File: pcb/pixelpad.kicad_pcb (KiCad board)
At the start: 2 copper layers, 61.5 x 55.5 mm, 17 parts, among them J1 OLED Display, SW1 SW_Push_45deg, SW2 SW_Push_45deg, SW3 RotaryEncoder_Switch, SW4 SW_Push_45deg, SW5 SW_Push_45deg, SW6 SW_Push_45deg, U1 MOUDLE-SEEEDUINO-XIAO

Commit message: The pins on the pcb for the oled were flipped for some reason
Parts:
- moved J1 7.50 mm to (59.0, 46.0), turned to 180 degrees
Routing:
- net GND: track 86.3 -> 89.6 mm, vias 2 -> 1
- net VCC: track 65.5 -> 66.5 mm
- net SDA: track 40.0 -> 39.2 mm, vias 0 -> 1
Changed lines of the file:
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@@
 	(footprint "Connector_PinHeader_2.54mm:PinHeader_1x04_P2.54mm_Vertical"
 		(layer "F.Cu")
-		(at 59 38.5)
+		(at 59 46 180)
 		(descr "Through hole straight pin header, 1x04, 2.54mm pitch, single row")
 		(tags "Through hole pin header THT 1x04 2.54mm single row")
@@
 		(duplicate_pad_numbers_are_jumpers no)
 		(fp_line
-			(start -1.38 -1.38)
-			(end 0 -1.38)
+			(start 1.38 1.27)
+			(end 1.38 9)
 			(stroke
 				(width 0.12)
@@
 		)
 		(fp_line
-			(start -1.38 0)
-			(end -1.38 -1.38)
+			(start -1.38 9)
+			(end 1.38 9)
 			(stroke
 				(width 0.12)
@@
 		(fp_line
 			(start -1.38 1.27)
-			(end -1.38 9)
+			(end 1.38 1.27)
 			(stroke
 				(width 0.12)
@@
 		(fp_line
 			(start -1.38 1.27)
-			(end 1.38 1.27)
+			(end -1.38 9)
 			(stroke
 				(width 0.12)
@@
 		)
 		(fp_line
-			(start -1.38 9)
-			(end 1.38 9)
+			(start -1.38 0)
+			(end -1.38 -1.38)
 			(stroke
 				(width 0.12)
@@
 		)
 		(fp_line
-			(start 1.38 1.27)
-			(end 1.38 9)
+			(start -1.38 -1.38)
+			(end 0 -1.38)
 			(stroke
 				(width 0.12)
@@
 		)
 		(fp_line
-			(start -1.27 -0.635)
-			(end -0.635 -1.27)
+			(start 1.27 8.89)
+			(end -1.27 8.89)
 			(stroke
 				(width 0.1)
@@
 		)
 		(fp_line
-			(start -1.27 8.89)
-			(end -1.27 -0.635)
+			(start 1.27 -1.27)
+			(end 1.27 8.89)
 			(stroke
 				(width 0.1)
@@
 		)
 		(fp_line
-			(start 1.27 -1.27)
-			(end 1.27 8.89)
+			(start -1.27 8.89)
+			(end -1.27 -0.635)
 			(stroke
 				(width 0.1)
@@
 		)
 		(fp_line
-			(start 1.27 8.89)
-			(end -1.27 8.89)
+			(start -1.27 -0.635)
+			(end -0.635 -1.27)
 			(stroke
 				(width 0.1)
@@
 		)
 		(pad "1" thru_hole rect
-			(at 0 0)
+			(at 0 0 180)
 			(size 1.7 1.7)
 			(drill 1)
@@
 		)
 		(pad "2" thru_hole circle
-			(at 0 2.54)
+			(at 0 2.54 180)
 			(size 1.7 1.7)
 			(drill 1)
@@
 		)
 		(pad "3" thru_hole circle
-			(at 0 5.08)
+			(at 0 5.08 180)
 			(size 1.7 1.7)
 			(drill 1)
@@
 		)
 		(pad "4" thru_hole circle
-			(at 0 7.62)
+			(at 0 7.62 180)
 			(size 1.7 1.7)
 			(drill 1)
@@
 	)
 	(segment
-		(start 63.947985 36.092015)
-		(end 59 41.04)
-		(width 0.2)
-		(layer "F.Cu")
-		(net "VCC")
-	)
-	(segment
 		(start 78.7645 36.092015)
 		(end 79.9145 37.242015)
@@
 		(net "VCC")
 	)
-	(segment
-		(start 78.7645 36.092015)
-		(end 63.947985 36.092015)
-		(width 0.2)
-		(layer "F.Cu")
-		(net "VCC")
-	)
 	(via
 		(at 111.5 42)
@@
 	)
 	(segment
+		(start 78.7645 36.092015)
+		(end 66.367985 36.092015)
+		(width 0.2)
+		(layer "B.Cu")
+		(net "VCC")
+	)
+	(segment
 		(start 111 42)
 		(end 111.5 42)
@@
 	)
 	(segment
-		(start 82.632485 42.5)
-		(end 101.5 42.5)
+		(start 66.367985 36.092015)
+		(end 59 43.46)
 		(width 0.2)
-		(layer "F.Cu")
-		(net "GND")
+		(layer "B.Cu")
+		(net "VCC")
 	)
 	(segment
-		(start 62.5 38.5)
-		(end 62.632015 38.632015)
+		(start 82.632485 42.5)
+		(end 101.5 42.5)
 		(width 0.2)
 		(layer "F.Cu")
@@
 		(net "GND")
 	)
-	(segment
-		(start 62.632015 38.632015)
-		(end 78.7645 38.632015)
-		(width 0.2)
-		(layer "F.Cu")
-		(net "GND")
-	)
-	(via
-		(at 62.5 38.5)
-		(size 0.6)
-		(drill 0.3)
-		(layers "F.Cu" "B.Cu")
-		(net "GND")
-	)
 	(via
 		(at 101.5 42.5)
@@
 	)
 	(segment
-		(start 62.5 38.5)
-		(end 59 38.5)
+		(start 65.867985 38.632015)
+		(end 59 45.5)
 		(width 0.2)
 		(layer "B.Cu")
@@
 	)
 	(segment
+		(start 59 45.5)
+		(end 59 46)
+		(width 0.2)
+		(layer "B.Cu")
+		(net "GND")
+	)
+	(segment
 		(start 114.600001 47.399999)
 		(end 114 48)
@@
 	)
 	(segment
+		(start 78.7645 38.632015)
+		(end 65.867985 38.632015)
+		(width 0.2)
+		(layer "B.Cu")
+		(net "GND")
+	)
+	(segment
 		(start 109.814343 48)
 		(end 104.314343 42.5)
@@
 	)
 	(segment
-		(start 60.08 42.5)
-		(end 59 43.58)
+		(start 60.58 42.5)
+		(end 59 40.92)
 		(width 0.2)
 		(layer "F.Cu")
@@
 	)
 	(segment
-		(start 63.5 42.5)
-		(end 60.08 42.5)
+		(start 64 42.5)
+		(end 60.58 42.5)
 		(width 0.2)
 		(layer "F.Cu")
@@
 	)
 	(via
-		(at 63.5 42.5)
+		(at 64 42.5)
 		(size 0.6)
 		(drill 0.3)
@@
 	)
 	(segment
-		(start 63.5 42.5)
-		(end 87.722485 42.5)
+		(start 87.722485 42.5)
+		(end 64 42.5)
 		(width 0.2)
 		(layer "B.Cu")
@@
 	)
 	(segment
-		(start 62.6 41.9)
-		(end 59 45.5)
+		(start 66.5 37.5)
+		(end 59.88 37.5)
 		(width 0.2)
-		(layer "B.Cu")
+		(layer "F.Cu")
 		(net "SDA")
 	)
 	(segment
-		(start 87.762484 40)
-		(end 75 40)
+		(start 59.88 37.5)
+		(end 59 38.38)
 		(width 0.2)
-		(layer "B.Cu")
+		(layer "F.Cu")
 		(net "SDA")
 	)
-	(segment
-		(start 73.1 41.9)
-		(end 62.6 41.9)
-		(width 0.2)
-		(layer "B.Cu")
+	(via
+		(at 66.5 37.5)
+		(size 0.6)
+		(drill 0.3)
+		(layers "F.Cu" "B.Cu")
 		(net "SDA")
 	)
@@
 	)
 	(segment
-		(start 75 40)
-		(end 73.1 41.9)
+		(start 66.517985 37.482015)
+		(end 66.5 37.5)
 		(width 0.2)
 		(layer "B.Cu")
@@
 	(segment
 		(start 87.881242 40.118758)
-		(end 87.762484 40)
+		(end 85.244499 37.482015)
+		(width 0.2)
+		(layer "B.Cu")
+		(net "SDA")
+	)
+	(segment
+		(start 85.244499 37.482015)
+		(end 66.517985 37.482015)
 		(width 0.2)
 		(layer "B.Cu")

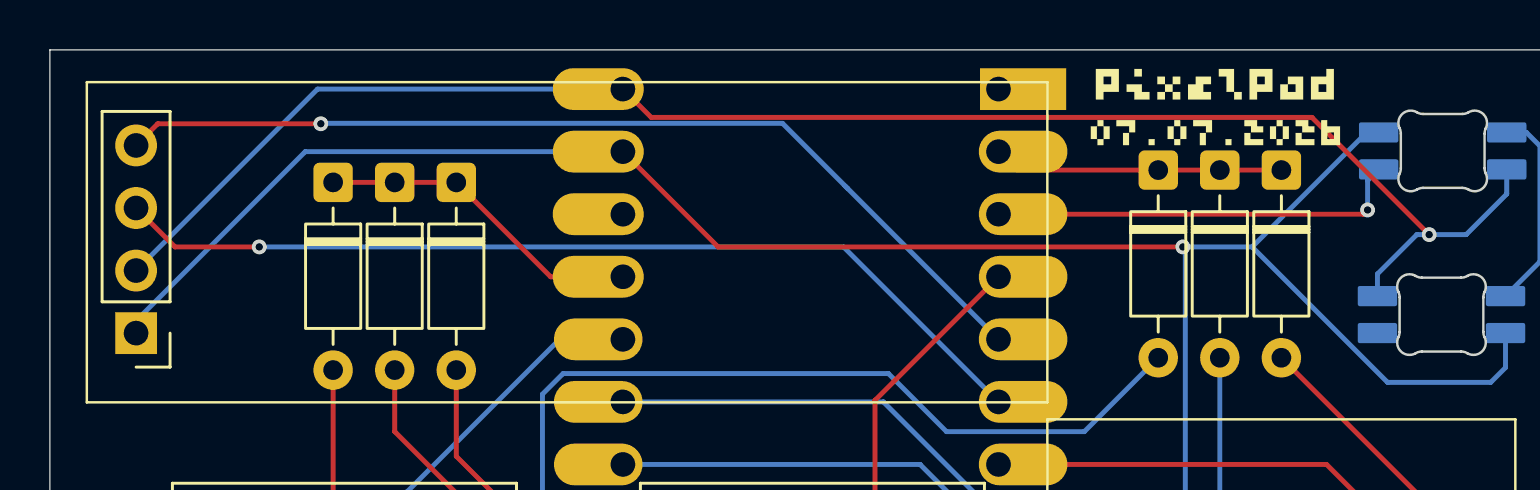
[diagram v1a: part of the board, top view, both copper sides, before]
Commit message: Cleaup tracks and vias
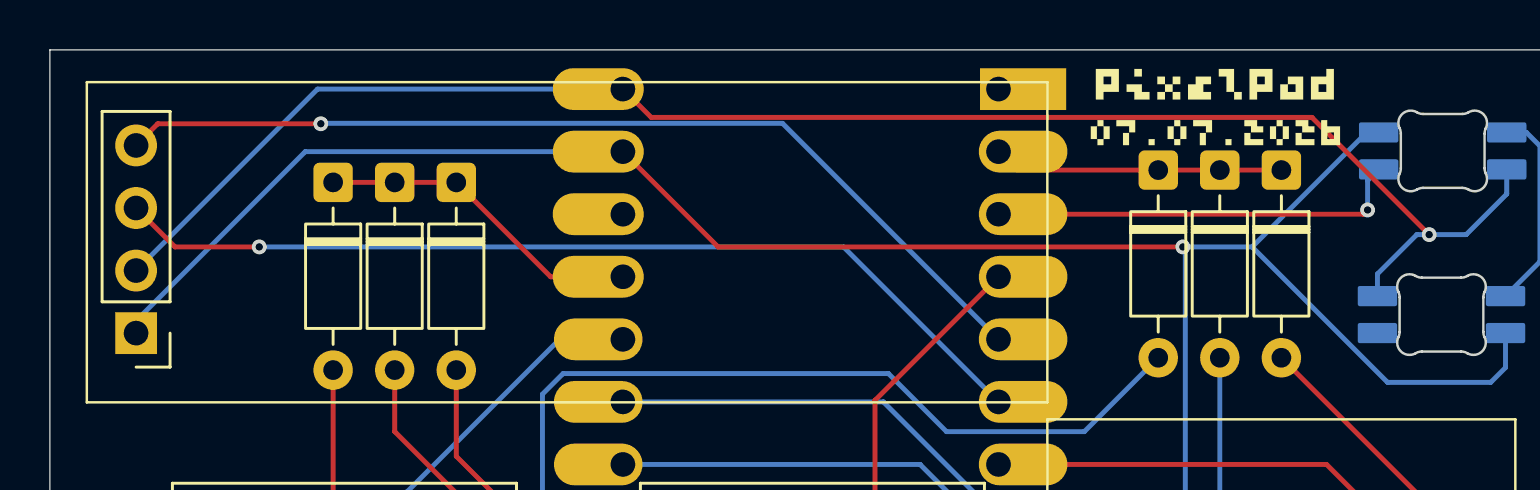
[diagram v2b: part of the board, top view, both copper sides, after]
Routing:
- net GND: track 89.6 -> 88.5 mm
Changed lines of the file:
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@@
-	)
-	(segment
-		(start 109.811499 37.852842)
-		(end 109.899999 37.852842)
-		(width 0.2)
-		(layer "B.Cu")
-		(net "GND")
-	)
-	(segment
-		(start 108.961501 37.852842)
-		(end 109.449999 37.852842)
-		(width 0.2)
-		(layer "B.Cu")
-		(net "GND")
 	)
 	(segment
@@
 		(start 101.5 42.5)
 		(end 101.6 42.6)
-		(width 0.2)
-		(layer "B.Cu")
-		(net "GND")
-	)
-	(segment
-		(start 59 45.5)
-		(end 59 46)
 		(width 0.2)
 		(layer "B.Cu")
@@
 	)
 	(segment
-		(start 87.881242 40.118758)
-		(end 87.7845 40.022015)
-		(width 0.2)
-		(layer "B.Cu")
-		(net "SDA")
-	)
-	(segment
-		(start 94.0145 46.252015)
-		(end 87.881242 40.118758)
-		(width 0.2)
-		(layer "B.Cu")
-		(net "SDA")
-	)
-	(segment
 		(start 66.517985 37.482015)
 		(end 66.5 37.5)
@@
 	)
 	(segment
-		(start 87.881242 40.118758)
-		(end 85.244499 37.482015)
-		(width 0.2)
-		(layer "B.Cu")
+		(start 85.244499 37.482015)
+		(end 94.0145 46.252015)
+		(width 0.2)
+		(layer "B.Cu")

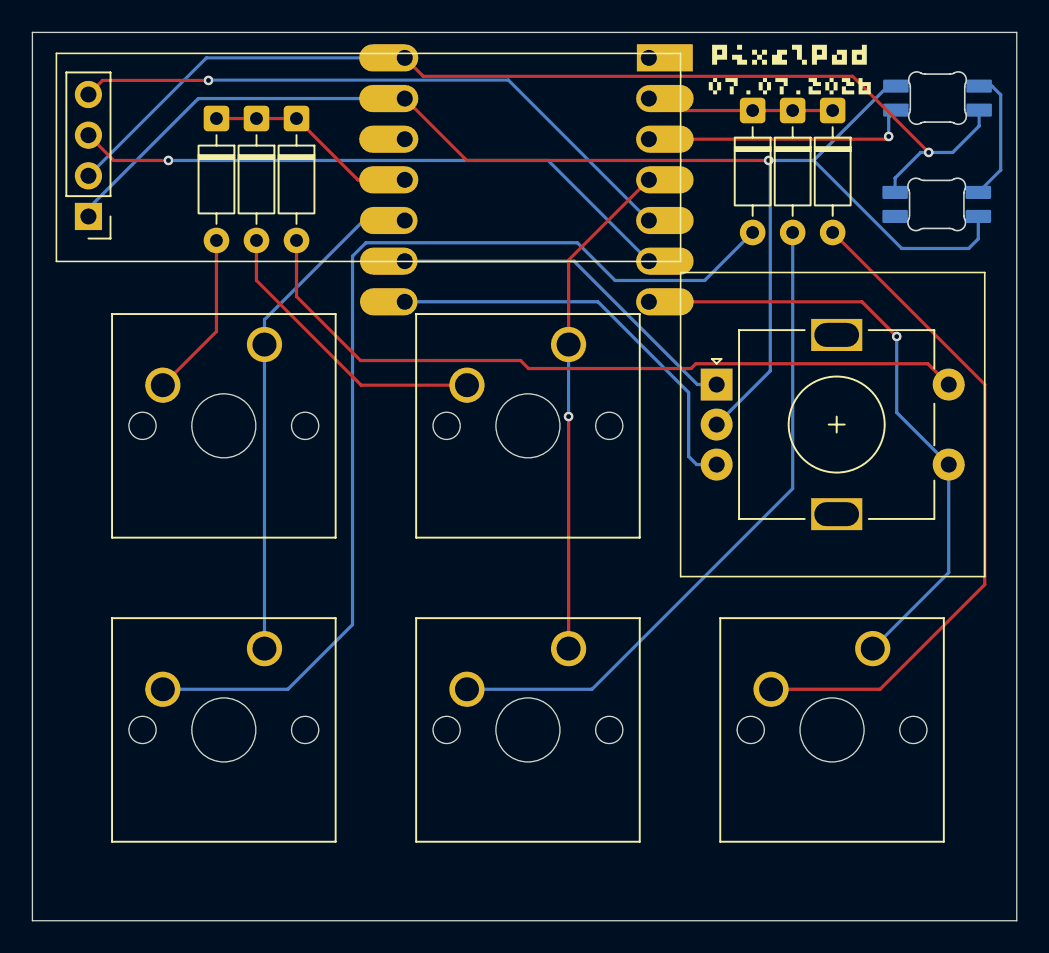
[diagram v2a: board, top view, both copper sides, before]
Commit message: Moved diodes around to make it more symmetric
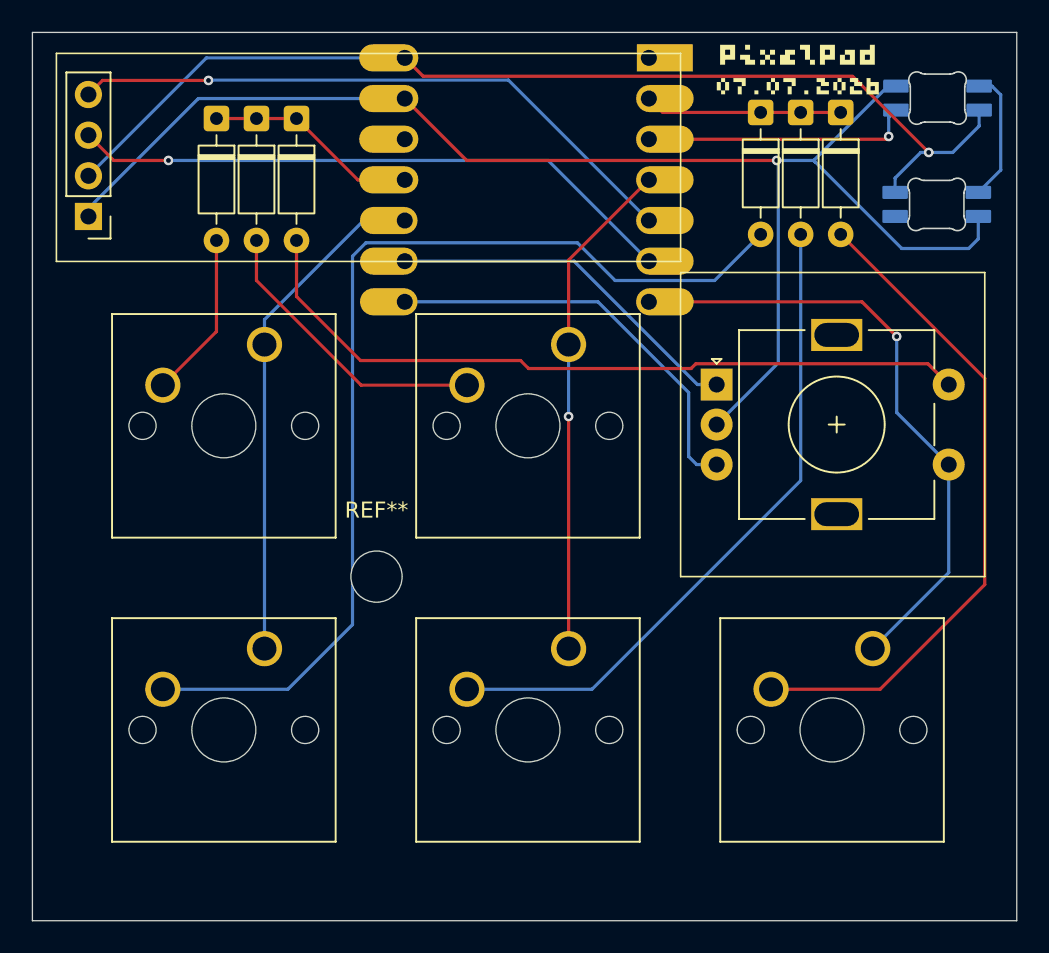
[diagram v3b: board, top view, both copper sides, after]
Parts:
- added REF**: MountingHole_3.2mm_M3, MountingHole:MountingHole_3.2mm_M3, F.Cu at (77.0, 68.5)
- moved D6 0.51 mm to (101.0, 39.5)
- moved D7 0.51 mm to (103.5, 39.5)
- moved D8 0.51 mm to (106.0, 39.5)
- moved G*** 0.50 mm to (103.5, 37.0)
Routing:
- net ROW1: track 10.7 -> 12.3 mm
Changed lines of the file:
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@@
 		)
 	)
+	(footprint "MountingHole:MountingHole_3.2mm_M3"
+		(layer "F.Cu")
+		(at 77 68.5)
+		(descr "Mounting Hole 3.2mm, M3, no annular, generated by kicad-footprint-generator mountinghole.py")
+		(tags "mountinghole M3")
+		(property "Reference" "REF**"
+			(at 0 -4.15 0)
+			(layer "F.SilkS")
+			(effects
+				(font
+					(size 1 1)
+					(thickness 0.15)
+				)
+			)
+		)
+		(property "Value" "MountingHole_3.2mm_M3"
+			(at 0 4.15 0)
+			(layer "F.Fab")
+			(effects
+				(font
+					(size 1 1)
+					(thickness 0.15)
+				)
+			)
+		)
+		(property "Datasheet" ""
+			(at 0 0 0)
+			(layer "F.Fab")
+			(hide yes)
+			(effects
+				(font
+					(size 1.27 1.27)
+				)
+			)
+		)
+		(property "Description" ""
+			(at 0 0 0)
+			(layer "F.Fab")
+			(hide yes)
+			(effects
+				(font
+					(size 1.27 1.27)
+				)
+			)
+		)
+		(property "KiLib_Generator" "mounting_hardware/mounting_hole"
+			(at 0 0 0)
+			(layer "F.SilkS")
+			(hide yes)
+			(effects
+				(font
+					(size 1 1)
+					(thickness 0.15)
+				)
+			)
+		)
+		(attr exclude_from_pos_files exclude_from_bom)
+		(duplicate_pad_numbers_are_jumpers no)
+		(fp_circle
+			(center 0 0)
+			(end 3.2 0)
+			(stroke
+				(width 0.15)
+				(type solid)
+			)
+			(fill no)
+			(layer "Cmts.User")
+		)
+		(fp_circle
+			(center 0 0)
+			(end 3.45 0)
+			(stroke
+				(width 0.05)
+				(type solid)
+			)
+			(fill no)
+			(layer "F.CrtYd")
+		)
+		(fp_text user "${REFERENCE}"
+			(at 0 0 0)
+			(layer "F.Fab")
+			(effects
+				(font
+					(size 1 1)
+					(thickness 0.15)
+				)
+			)
+		)
+		(pad "" np_thru_hole circle
+			(at 0 0)
+			(size 3.2 3.2)
+			(drill 3.2)
+			(layers "*.Cu" "*.Mask")
+		)
+		(embedded_fonts no)
+	)
 	(footprint "XIAO:SK6812MINI-E_fixed"
 		(layer "F.Cu")
@@
 	(footprint "Diode_THT:D_DO-35_SOD27_P7.62mm_Horizontal"
 		(layer "F.Cu")
-		(at 100.5 39.38 -90)
+		(at 101 39.5 -90)
 		(descr "Diode, DO-35_SOD27 series, Axial, Horizontal, pin pitch=7.62mm, length*diameter=4*2mm^2, http://www.diodes.com/_files/packages/DO-35.pdf")
 		(tags "Diode DO-35_SOD27 series Axial Horizontal pin pitch 7.62mm  length 4mm diameter 2mm")
@@
 	(footprint "Diode_THT:D_DO-35_SOD27_P7.62mm_Horizontal"
 		(layer "F.Cu")
-		(at 103 39.38 -90)
+		(at 103.5 39.5 -90)
 		(descr "Diode, DO-35_SOD27 series, Axial, Horizontal, pin pitch=7.62mm, length*diameter=4*2mm^2, http://www.diodes.com/_files/packages/DO-35.pdf")
 		(tags "Diode DO-35_SOD27 series Axial Horizontal pin pitch 7.62mm  length 4mm diameter 2mm")
@@
 	(footprint "Diode_THT:D_DO-35_SOD27_P7.62mm_Horizontal"
 		(layer "F.Cu")
-		(at 105.5 39.38 -90)
+		(at 106 39.5 -90)
 		(descr "Diode, DO-35_SOD27 series, Axial, Horizontal, pin pitch=7.62mm, length*diameter=4*2mm^2, http://www.diodes.com/_files/packages/DO-35.pdf")
 		(tags "Diode DO-35_SOD27 series Axial Horizontal pin pitch 7.62mm  length 4mm diameter 2mm")
@@
 	(footprint "silkscreen:silkscreen"
 		(layer "F.Cu")
-		(at 103 37)
+		(at 103.5 37)
 		(property "Reference" "G***"
 			(at 0 0 0)
@@
 	(segment
 		(start 82.632485 42.5)
-		(end 101.5 42.5)
+		(end 78.7645 38.632015)
 		(width 0.2)
 		(layer "F.Cu")
@@
 	)
 	(segment
-		(start 78.7645 38.632015)
+		(start 102 42.5)
 		(end 82.632485 42.5)
 		(width 0.2)
@@
 	)
 	(via
-		(at 101.5 42.5)
+		(at 102 42.5)
 		(size 0.6)
 		(drill 0.3)
@@
 	)
 	(segment
+		(start 98.25 59)
+		(end 102.1 55.15)
+		(width 0.2)
+		(layer "B.Cu")
+		(net "GND")
+	)
+	(segment
 		(start 65.867985 38.632015)
 		(end 59 45.5)
@@
 	)
 	(segment
-		(start 114.600001 45.997158)
-		(end 114.600001 47.399999)
+		(start 104.407171 42.592829)
+		(end 104.314343 42.5)
 		(width 0.2)
 		(layer "B.Cu")
@@
 	)
 	(segment
-		(start 101.5 42.5)
-		(end 101.6 42.6)
+		(start 114.600001 45.997158)
+		(end 114.600001 47.399999)
 		(width 0.2)
 		(layer "B.Cu")
@@
 	)
 	(segment
-		(start 101.6 55.65)
-		(end 98.25 59)
+		(start 104.314342 42.5)
+		(end 102 42.5)
 		(width 0.2)
 		(layer "B.Cu")
@@
 	(segment
 		(start 109.814343 48)
-		(end 104.314343 42.5)
+		(end 104.407171 42.592829)
 		(width 0.2)
 		(layer "B.Cu")
@@
 	)
 	(segment
+		(start 102.1 55.15)
+		(end 102.1 42.6)
+		(width 0.2)
+		(layer "B.Cu")
+		(net "GND")
+	)
+	(segment
 		(start 114 48)
 		(end 109.814343 48)
@@
 	)
 	(segment
-		(start 101.6 42.6)
-		(end 101.6 55.65)
+		(start 102.1 42.6)
+		(end 102 42.5)
 		(width 0.2)
 		(layer "B.Cu")
@@
 	)
 	(segment
-		(start 104.314343 42.5)
-		(end 101.5 42.5)
+		(start 104.407171 42.592829)
+		(end 104.314342 42.5)
 		(width 0.2)
 		(layer "B.Cu")
@@
 	)
 	(segment
-		(start 100.5 39.38)
-		(end 103 39.38)
-		(width 0.2)
-		(layer "F.Cu")
-		(net "ROW1")
-	)
-	(segment
-		(start 94.762485 39.38)
-		(end 100.5 39.38)
+		(start 94.882485 39.5)
+		(end 106 39.5)
 		(width 0.2)
 		(layer "F.Cu")
@@
 	)
 	(segment
-		(start 103 39.38)
-		(end 105.5 39.38)
+		(start 94.0145 38.632015)
+		(end 94.882485 39.5)
 		(width 0.2)
 		(layer "F.Cu")
@@
 	)
 	(segment
-		(start 75.5 71.5)
-		(end 71.46 75.54)
+		(start 91.903921 50)
+		(end 98.12 50)
 		(width 0.2)
 		(layer "B.Cu")
@@
 	)
 	(segment
-		(start 76.338154 47.642015)
-		(end 75.5 48.480169)
+		(start 98.12 50)
+		(end 101 47.12)
 		(width 0.2)
 		(layer "B.Cu")
@@
 	)
 	(segment
-		(start 100.5 47)
-		(end 97.5 50)
+		(start 63.65 75.54)
+		(end 71.46 75.54)
 		(width 0.2)
 		(layer "B.Cu")
@@
 	)
 	(segment
-		(start 97.5 50)
-		(end 91.903921 50)
+		(start 75.5 71.5)
+		(end 75.5 48.480169)
 		(width 0.2)
 		(layer "B.Cu")
@@
 	)
 	(segment
-		(start 91.903921 50)
+		(start 76.338154 47.642015)
 		(end 89.545936 47.642015)
 		(width 0.2)
@@
 	(segment
 		(start 89.545936 47.642015)
-		(end 76.338154 47.642015)
+		(end 91.903921 50)
 		(width 0.2)
 		(layer "B.Cu")
@@
 	(segment
 		(start 71.46 75.54)
-		(end 63.65 75.54)
+		(end 75.5 71.5)
 		(width 0.2)
 		(layer "B.Cu")
@@
 	(segment
 		(start 75.5 48.480169)
-		(end 75.5 71.5)
+		(end 76.338154 47.642015)
 		(width 0.2)
 		(layer "B.Cu")
@@
 	)
 	(segment
-		(start 103 47)
-		(end 103 63)
+		(start 103.5 47.12)
+		(end 103.5 62.5)
 		(width 0.2)
 		(layer "B.Cu")
@@
 	)
 	(segment
-		(start 103 63)
+		(start 103.5 62.5)
 		(end 90.46 75.54)
 		(width 0.2)
@@
 	)
 	(segment
-		(start 105.5 47)
-		(end 115 56.5)
+		(start 108.46 75.54)
+		(end 101.65 75.54)
 		(width 0.2)
 		(layer "F.Cu")
@@
 	)
 	(segment
-		(start 115 69)
-		(end 108.46 75.54)
+		(start 106 47.12)
+		(end 115 56.12)
 		(width 0.2)
 		(layer "F.Cu")
@@
 	)
 	(segment
-		(start 115 56.5)
-		(end 115 69)
+		(start 115 69)
+		(end 108.46 75.54)
 		(width 0.2)
 		(layer "F.Cu")
@@
 	)
 	(segment
-		(start 108.46 75.54)
-		(end 101.65 75.54)
+		(start 115 56.12)
+		(end 115 69)
 		(width 0.2)
 		(layer "F.Cu")
